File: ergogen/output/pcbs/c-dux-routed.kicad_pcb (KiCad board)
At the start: 2 copper layers, 147.3 x 116.9 mm, 25 parts, among them SW1 SW_Push_Lock, SW2 SW-SMD_4P

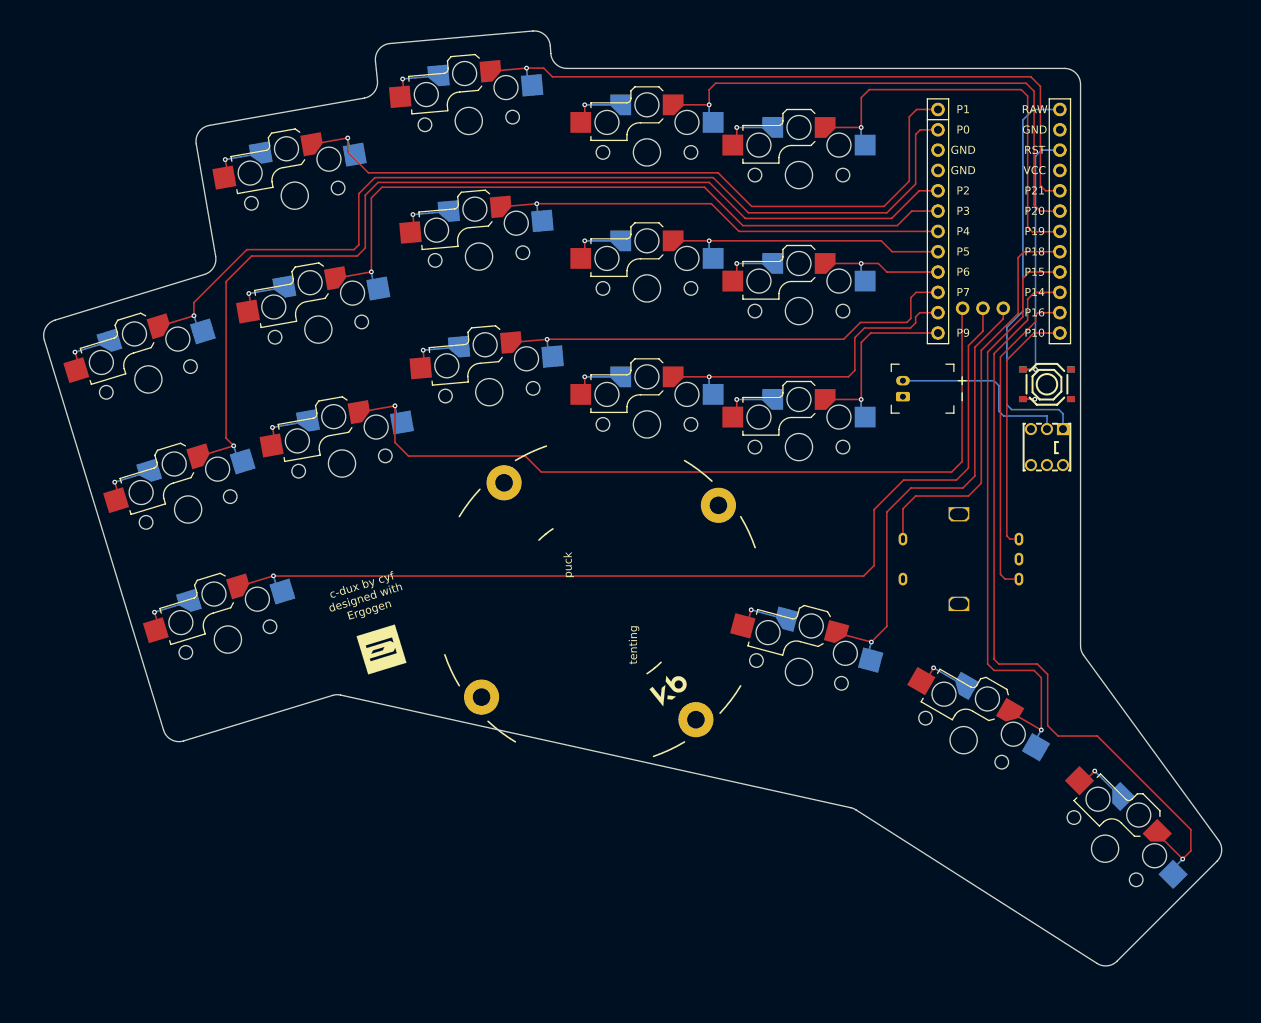
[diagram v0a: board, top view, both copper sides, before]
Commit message: kicad: finish routing.
With some manual placement change after routing almost done.
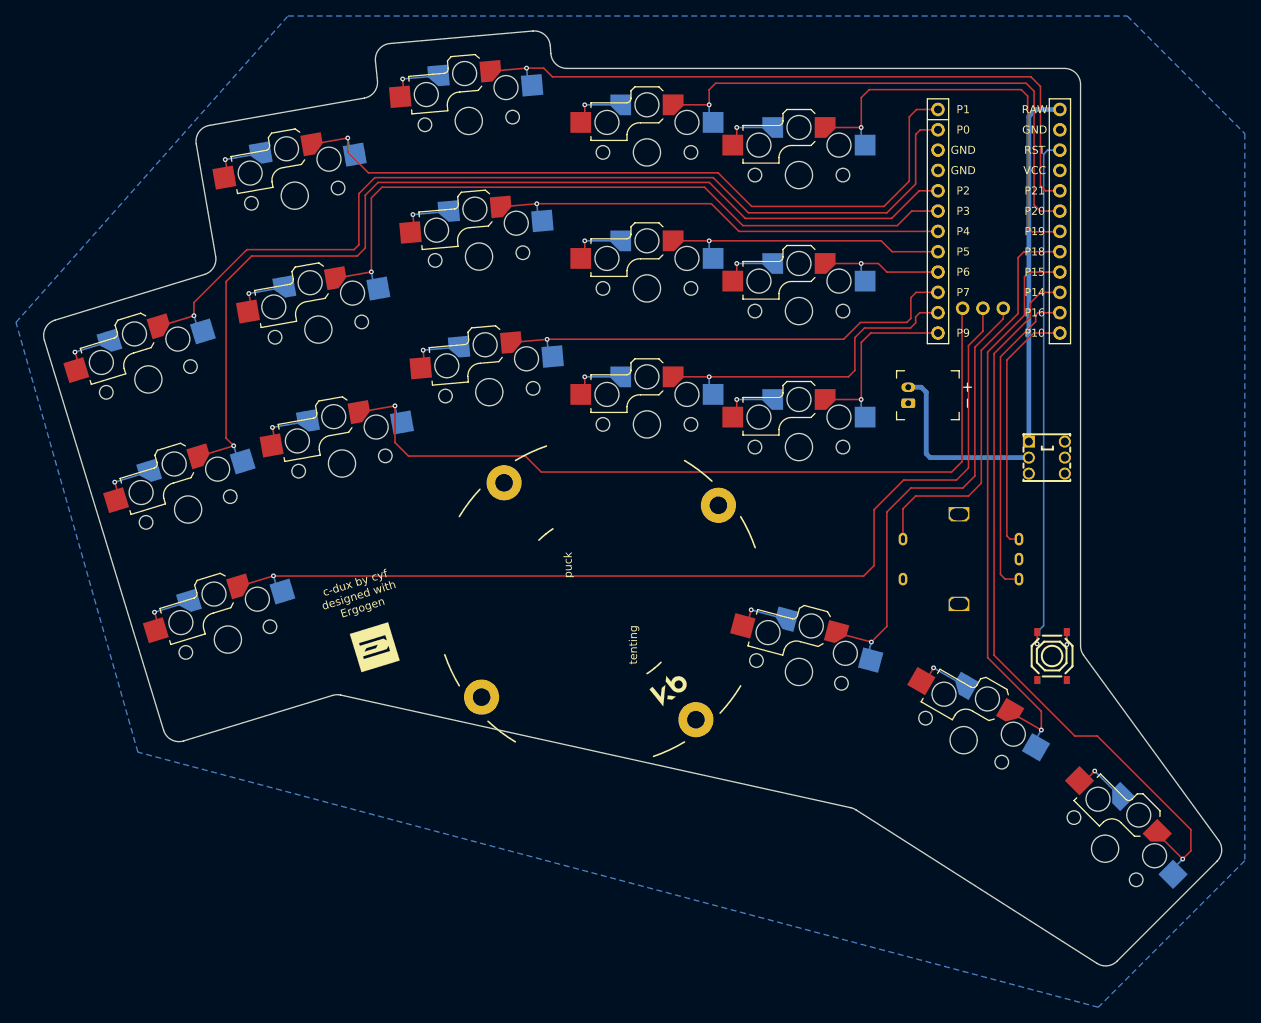
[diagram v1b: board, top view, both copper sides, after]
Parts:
- moved SW2 34.0 mm to (248.1, 152.8), turned to -90 degrees
- moved SW1 1.32 mm to (247.4, 128.0), turned to 90 degrees
- moved JST1 1.05 mm to (230.1, 120.2)
- moved LOGO1 0.89 mm to (163.4, 151.7)
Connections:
- SW2 pad 1: RST -> GND
- SW2 pad 3: GND -> RST
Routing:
- net RST: track 33.2 -> 65.4 mm
- net RAW: track 51.0 -> 44.9 mm
- net P14: track 99.1 -> 94.6 mm
- net P15: track 75.6 -> 72.7 mm
- added copper zone on B.Cu, net GND

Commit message: kicad: fill copper zone for both sides, add tear drops.
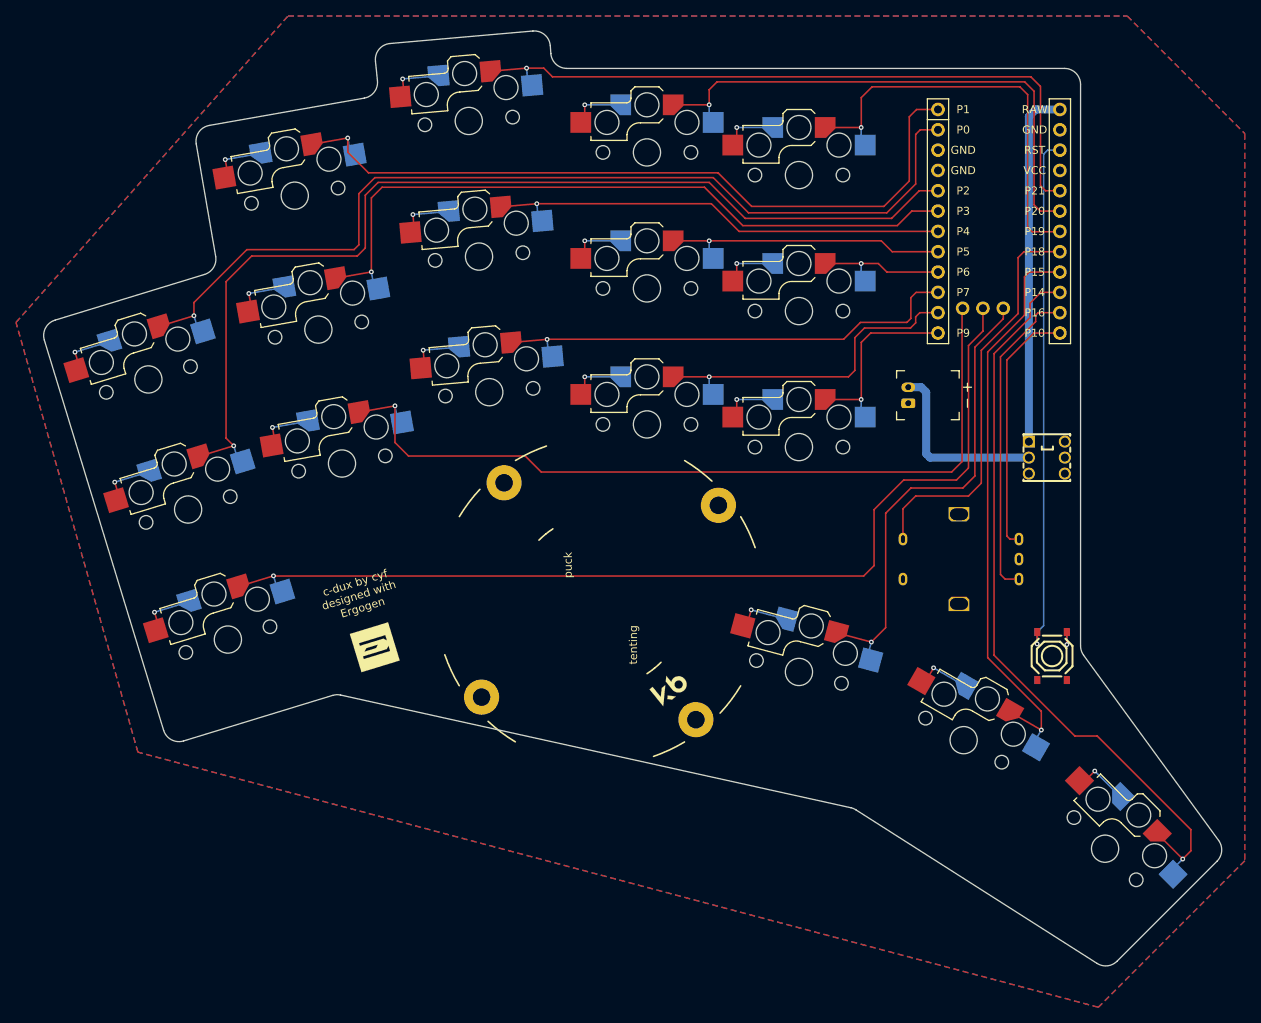
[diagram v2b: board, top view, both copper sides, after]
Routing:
- added copper zone on F.Cu, net GND

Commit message: kicad: manually remove unnecessary GND line on F.cu layer.
After copper filling for F.cu, GND lines for choc hotswap socket become
unnecessary and they have a very small gap with copper filling
connection to PTH. Thus manually remove them to avoid potential
problems.

The problem could be fixed by changing ceoloide/switch_choc_v1_v2.js to
add some offset for the via hole.
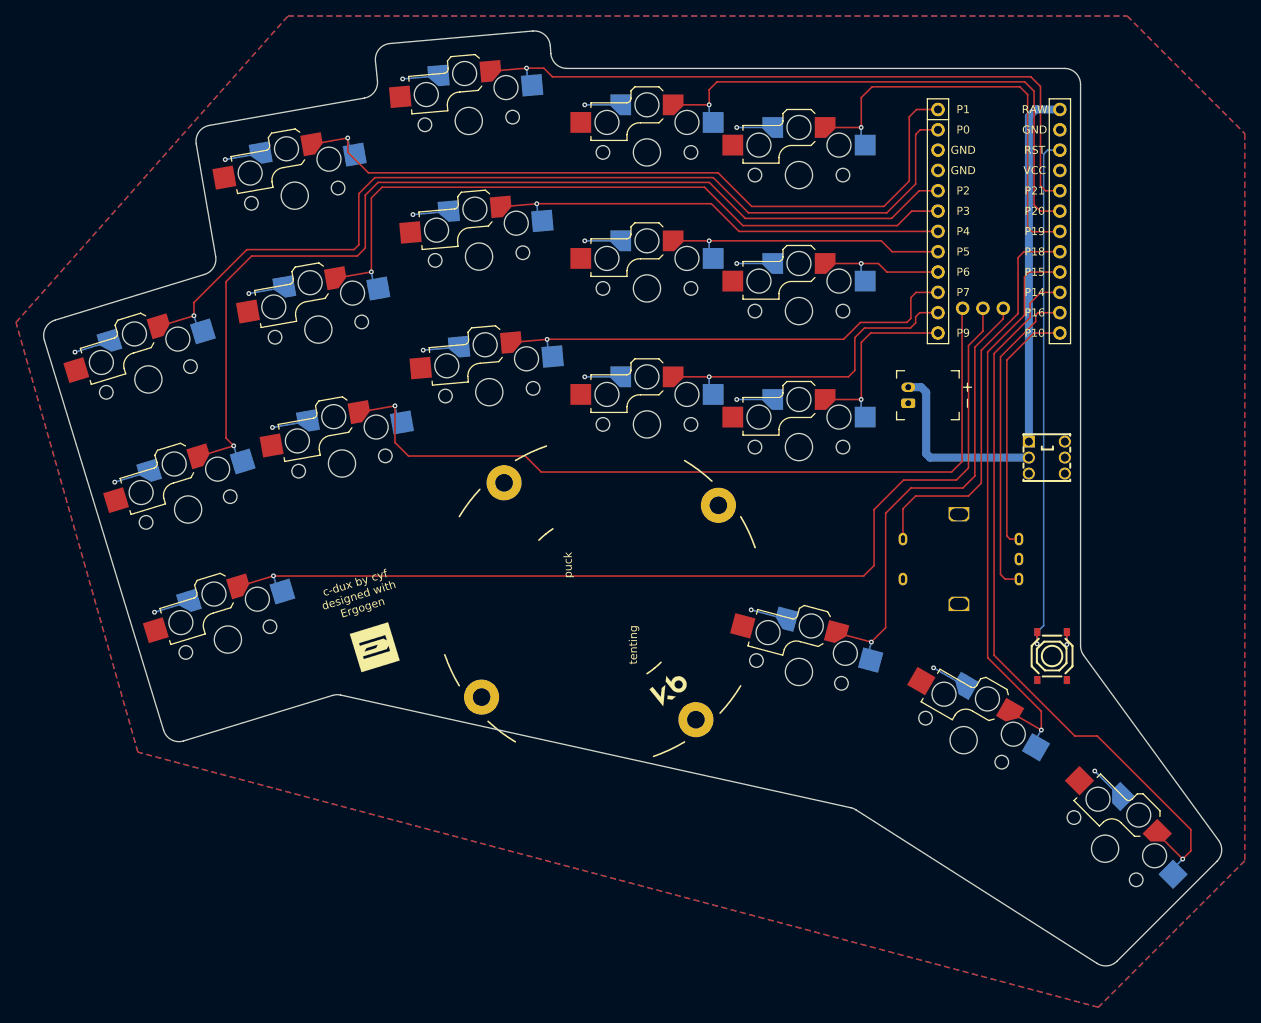
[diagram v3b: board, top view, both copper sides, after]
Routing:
- net GND: track 123.7 -> 84.1 mm
